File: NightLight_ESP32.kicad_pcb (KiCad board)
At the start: 2 copper layers, 38.1 x 43.2 mm, 27 parts, among them J1 USB_C_Receptacle_USB2.0, J2 BUTTON, Q1 MMBT2222, Q2 MMBT2222, SW1 TL3342, SW2 TL3342, U1 ESP32-WROOM-32D, U2 AP2112K-3.3, U3 CH340C

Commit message: Updated to v6
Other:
- net class Default removed

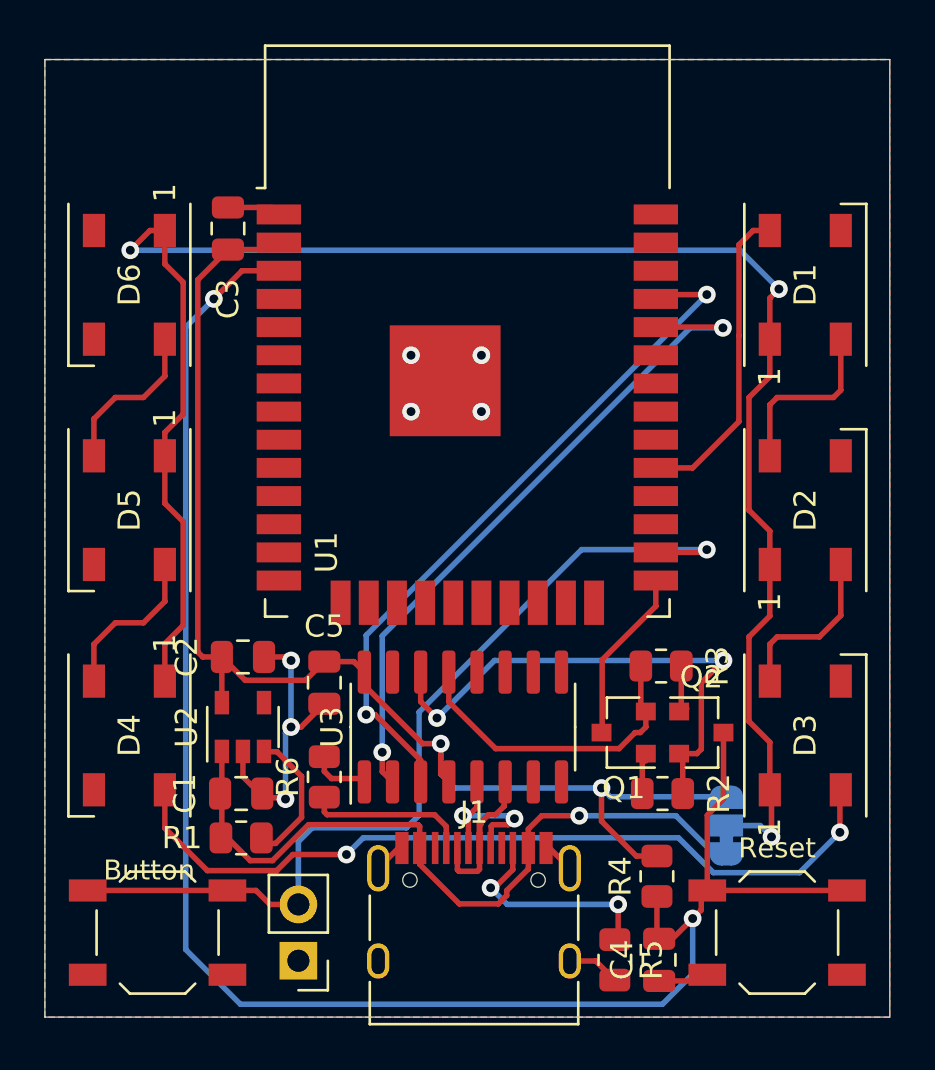
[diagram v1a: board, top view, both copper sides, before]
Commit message: Fix some DRC errors
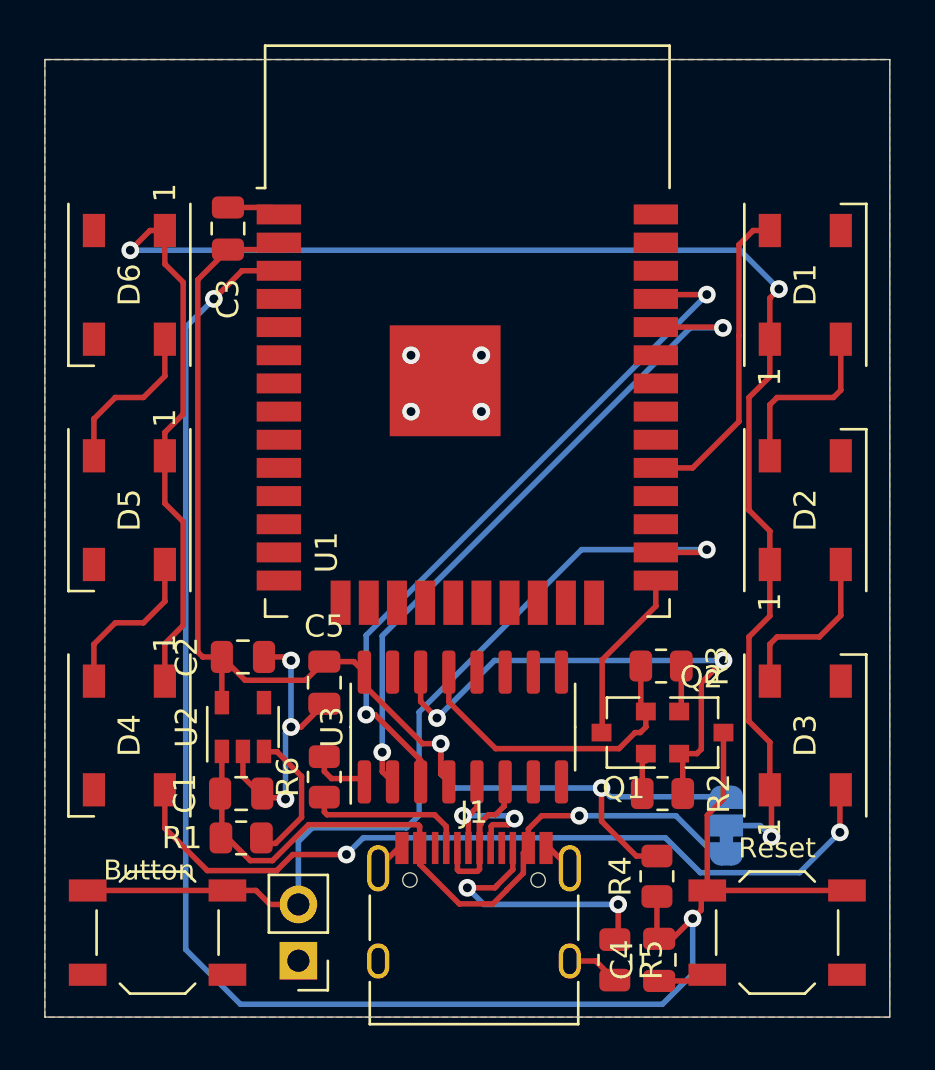
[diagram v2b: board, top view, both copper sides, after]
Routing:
- net Net-(J1-PadB5): track 9.96 -> 12.1 mm
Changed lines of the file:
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@@
   (segment (start 137.16 104.775) (end 140.335 104.775) (width 0.25) (layer "B.Cu") (net 1))
   (segment (start 131.75 116) (end 131.75 119) (width 0.25) (layer "B.Cu") (net 1))
-  (segment (start 137.55 125.18641) (end 139.338592 126.975002) (width 0.25) (layer "F.Cu") (net 2))
+  (segment (start 141.475002 126.341394) (end 142.225 125.591396) (width 0.25) (layer "F.Cu") (net 2))
   (segment (start 142.45 123.601833) (end 143.051833 123) (width 0.25) (layer "F.Cu") (net 2))
-  (segment (start 141.098002 126.975002) (end 141.475002 126.598002) (width 0.25) (layer "F.Cu") (net 2))
   (segment (start 142.45 124.455) (end 142.45 123.601833) (width 0.25) (layer "F.Cu") (net 2))
   (segment (start 137.474999 123.404999) (end 137.55 123.48) (width 0.25) (layer "F.Cu") (net 2))
   (segment (start 132.533191 123.404999) (end 137.474999 123.404999) (width 0.25) (layer "F.Cu") (net 2))
-  (segment (start 142.45 125.398675) (end 142.45 124.455) (width 0.25) (layer "F.Cu") (net 2))
+  (segment (start 139.338592 126.975002) (end 140.855394 126.975002) (width 0.25) (layer "F.Cu") (net 2))
+  (segment (start 142.225 125.591396) (end 142.225 124.68) (width 0.25) (layer "F.Cu") (net 2))
+  (segment (start 140.855394 126.975002) (end 141.475002 126.355394) (width 0.25) (layer "F.Cu") (net 2))
   (segment (start 143.051833 123) (end 144.75 123) (width 0.25) (layer "F.Cu") (net 2))
-  (segment (start 141.475002 126.373673) (end 142.45 125.398675) (width 0.25) (layer "F.Cu") (net 2))
   (segment (start 128.63 120.115) (end 128.63 123.74319) (width 0.25) (layer "F.Cu") (net 2))
-  (segment (start 141.475002 126.598002) (end 141.475002 126.373673) (width 0.25) (layer "F.Cu") (net 2))
   (segment (start 137.55 124.455) (end 137.55 125.18641) (width 0.25) (layer "F.Cu") (net 2))
+  (segment (start 137.55 125.18641) (end 139.338592 126.975002) (width 0.25) (layer "F.Cu") (net 2))
+  (segment (start 142.225 124.68) (end 142.45 124.455) (width 0.25) (layer "F.Cu") (net 2))
   (segment (start 137.55 123.48) (end 137.55 124.455) (width 0.25) (layer "F.Cu") (net 2))
   (segment (start 129.91182 125.02501) (end 130.91318 125.02501) (width 0.25) (layer "F.Cu") (net 2))
+  (segment (start 141.475002 126.355394) (end 141.475002 126.341394) (width 0.25) (layer "F.Cu") (net 2))
   (segment (start 128.63 123.74319) (end 129.91182 125.02501) (width 0.25) (layer "F.Cu") (net 2))
-  (segment (start 139.338592 126.975002) (end 141.098002 126.975002) (width 0.25) (layer "F.Cu") (net 2))
   (segment (start 130.91318 125.02501) (end 132.533191 123.404999) (width 0.25) (layer "F.Cu") (net 2))
   (via (at 144.75 123) (size 0.8) (drill 0.4) (layers "F.Cu" "B.Cu") (net 2))
@@
   (segment (start 150.848998 124.744) (end 151.384 124.744) (width 0.25) (layer "B.Cu") (net 2))
   (segment (start 128.63 117.915) (end 128.63 115.84) (width 0.25) (layer "F.Cu") (net 3))
-  (segment (start 128.564 115.84) (end 128.63 115.84) (width 0.25) (layer "F.Cu") (net 3))
   (segment (start 145.75 123.2475) (end 145.75 121.75) (width 0.25) (layer "F.Cu") (net 3))
   (segment (start 127.544999 115.615001) (end 127.769998 115.84) (width 0.25) (layer "F.Cu") (net 3))
@@
   (segment (start 150.52 126.37) (end 156.82 126.37) (width 0.25) (layer "F.Cu") (net 4))
   (segment (start 129.53999 98.425) (end 128.27 99.69499) (width 0.25) (layer "F.Cu") (net 4))
-  (segment (start 148.21 128.59) (end 148.25 128.55) (width 0.25) (layer "F.Cu") (net 4))
   (segment (start 148.944988 128.55) (end 149.859988 127.635) (width 0.25) (layer "F.Cu") (net 4))
   (segment (start 148.25 126.6425) (end 148.25 128.3) (width 0.25) (layer "F.Cu") (net 4))
@@
   (via (at 134.25 124.75) (size 0.8) (drill 0.4) (layers "F.Cu" "B.Cu") (net 8))
   (via (at 156.5 123.75) (size 0.8) (drill 0.4) (layers "F.Cu" "B.Cu") (net 8))
-  (segment (start 149.221652 123.99499) (end 150.795672 125.56901) (width 0.25) (layer "B.Cu") (net 8))
   (segment (start 154.68099 125.56901) (end 156.5 123.75) (width 0.25) (layer "B.Cu") (net 8))
+  (segment (start 135.00501 123.99499) (end 148.63299 123.99499) (width 0.25) (layer "B.Cu") (net 8))
+  (segment (start 150.20701 125.56901) (end 154.68099 125.56901) (width 0.25) (layer "B.Cu") (net 8))
+  (segment (start 148.63299 123.99499) (end 150.20701 125.56901) (width 0.25) (layer "B.Cu") (net 8))
   (segment (start 134.25 124.75) (end 135.00501 123.99499) (width 0.25) (layer "B.Cu") (net 8))
-  (segment (start 135.00501 123.99499) (end 149.221652 123.99499) (width 0.25) (layer "B.Cu") (net 8))
-  (segment (start 150.795672 125.56901) (end 154.68099 125.56901) (width 0.25) (layer "B.Cu") (net 8))
   (segment (start 125.095 114.3) (end 126.06 113.335) (width 0.25) (layer "F.Cu") (net 9))
   (segment (start 122.86 115.265) (end 123.825 114.3) (width 0.25) (layer "F.Cu") (net 9))
@@
   (segment (start 136.955021 123.544979) (end 132.705021 123.544979) (width 0.25) (layer "B.Cu") (net 12))
   (segment (start 144.84952 111) (end 137.524999 118.324521) (width 0.25) (layer "B.Cu") (net 12))
-  (segment (start 132.08 125.797919) (end 132.08 127) (width 0.25) (layer "B.Cu") (net 12))
+  (segment (start 132.08 124.17) (end 132.08 127) (width 0.25) (layer "B.Cu") (net 12))
   (segment (start 132.705021 123.544979) (end 132.08 124.17) (width 0.25) (layer "B.Cu") (net 12))
   (segment (start 137.524999 122.975001) (end 136.955021 123.544979) (width 0.25) (layer "B.Cu") (net 12))
   (segment (start 150.5 111) (end 144.84952 111) (width 0.25) (layer "B.Cu") (net 12))
-  (segment (start 132.08 124.17) (end 132.08 125.797919) (width 0.25) (layer "B.Cu") (net 12))
-  (segment (start 147.7725 118.1725) (end 147.78 118.18) (width 0.25) (layer "F.Cu") (net 13))
   (segment (start 140.975001 119.975001) (end 138.865 117.865) (width 0.25) (layer "F.Cu") (net 13))
   (segment (start 138.865 117.865) (end 138.865 116.525) (width 0.25) (layer "F.Cu") (net 13))
@@
   (segment (start 138.224988 122.954988) (end 133.373738 122.954988) (width 0.25) (layer "F.Cu") (net 21))
   (segment (start 138.75 124.455) (end 138.75 123.48) (width 0.25) (layer "F.Cu") (net 21))
-  (segment (start 141.75 125.43) (end 140.93 126.25) (width 0.25) (layer "F.Cu") (net 22))
+  (segment (start 139.7 126.25) (end 140.944 126.25) (width 0.25) (layer "F.Cu") (net 22))
+  (segment (start 141.025002 126.154998) (end 141.75 125.43) (width 0.25) (layer "F.Cu") (net 22))
+  (segment (start 141.025002 126.168998) (end 141.025002 126.154998) (width 0.25) (layer "F.Cu") (net 22))
   (segment (start 146.5 127) (end 146.5 128.5875) (width 0.25) (layer "F.Cu") (net 22))
-  (segment (start 140.93 126.25) (end 140.75 126.25) (width 0.25) (layer "F.Cu") (net 22))
-  (segment (start 141.75 124.455) (end 141.75 125.43) (width 0.25) (layer "F.Cu") (net 22))
+  (segment (start 140.944 126.25) (end 141.025002 126.168998) (width 0.25) (layer "F.Cu") (net 22))
+  (segment (start 141.75 125.43) (end 141.75 124.455) (width 0.25) (layer "F.Cu") (net 22))
   (via (at 146.5 127) (size 0.8) (drill 0.4) (layers "F.Cu" "B.Cu") (net 22))
-  (via (at 140.75 126.25) (size 0.8) (drill 0.4) (layers "F.Cu" "B.Cu") (net 22))
-  (segment (start 141.5 127) (end 146.5 127) (width 0.25) (layer "B.Cu") (net 22))
-  (segment (start 140.75 126.25) (end 141.5 127) (width 0.25) (layer "B.Cu") (net 22))
+  (via (at 139.7 126.25) (size 0.8) (drill 0.4) (layers "F.Cu" "B.Cu") (net 22))
+  (segment (start 140.45 127) (end 146.5 127) (width 0.25) (layer "B.Cu") (net 22))
+  (segment (start 139.7 126.25) (end 140.45 127) (width 0.25) (layer "B.Cu") (net 22))
   (segment (start 147.5875 122) (end 147.5875 120.53001) (width 0.25) (layer "F.Cu") (net 23))
   (segment (start 147.5875 120.53001) (end 147.75 120.53001) (width 0.25) (layer "F.Cu") (net 23))
   (segment (start 149.3475 115.955) (end 149.3475 118.1725) (width 0.25) (layer "F.Cu") (net 24))
-  (segment (start 149.5975 118.1725) (end 149.59 118.18) (width 0.25) (layer "F.Cu") (net 24))
-  (segment (start 149.6425 116) (end 149.5975 115.955) (width 0.25) (layer "F.Cu") (net 24))
   (zone (net 1) (net_name "GND") (layer "F.Cu") (hatch edge 0.508)
     (connect_pads (clearance 0.508))
-    (min_thickness 0.254)
+    (min_thickness 0.254) (filled_areas_thickness no)
     (fill yes (thermal_gap 0.508) (thermal_bridge_width 0.508))
     (polygon
@@
     (connect_pads (clearance 0))
     (min_thickness 0.254)
-    (keepout (tracks not_allowed) (vias not_allowed) (pads allowed) (copperpour not_allowed) (footprints allowed))
+    (keepout (tracks not_allowed) (vias not_allowed) (pads allowed ) (copperpour not_allowed) (footprints allowed))
     (fill (thermal_gap 0.508) (thermal_bridge_width 0.508))
     (polygon
@@
   (zone (net 1) (net_name "GND") (layer "B.Cu") (hatch edge 0.508)
     (connect_pads (clearance 0.508))
-    (min_thickness 0.254)
+    (min_thickness 0.254) (filled_areas_thickness no)
     (fill yes (thermal_gap 0.508) (thermal_bridge_width 0.508))
     (polygon
